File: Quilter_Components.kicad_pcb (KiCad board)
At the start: 4 copper layers, 40.4 x 100 mm, 146 parts, among them J1 Conn_01x10_Male, J2 Conn_01x10_Male, J3 Conn_01x10_Male, J4 Eurorack_10_pin_power, U1 TL072, U10 SSI2144, U2 TL074, U3 TL074, U4 TL074, U5 SSI2144, U7 SSI2144, U9 SSI2144

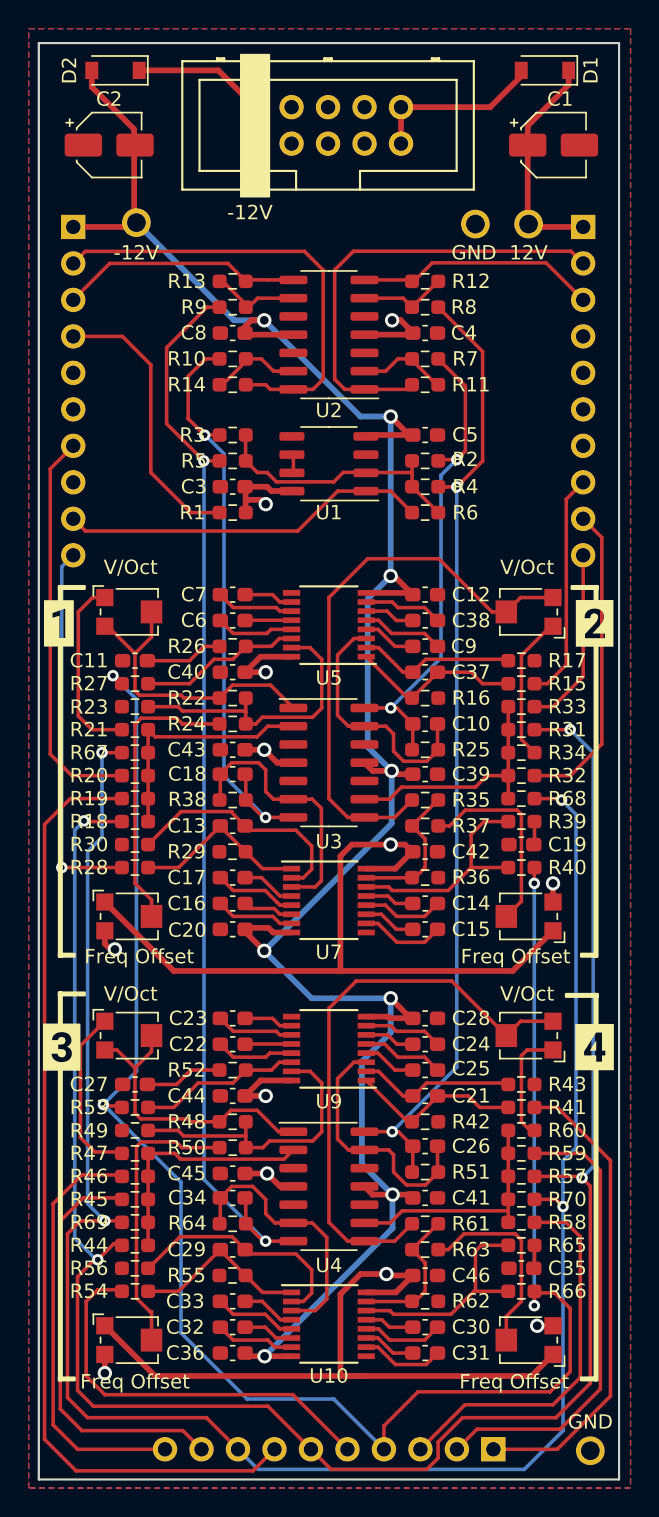
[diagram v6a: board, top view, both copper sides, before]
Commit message: Finished routing components and controls
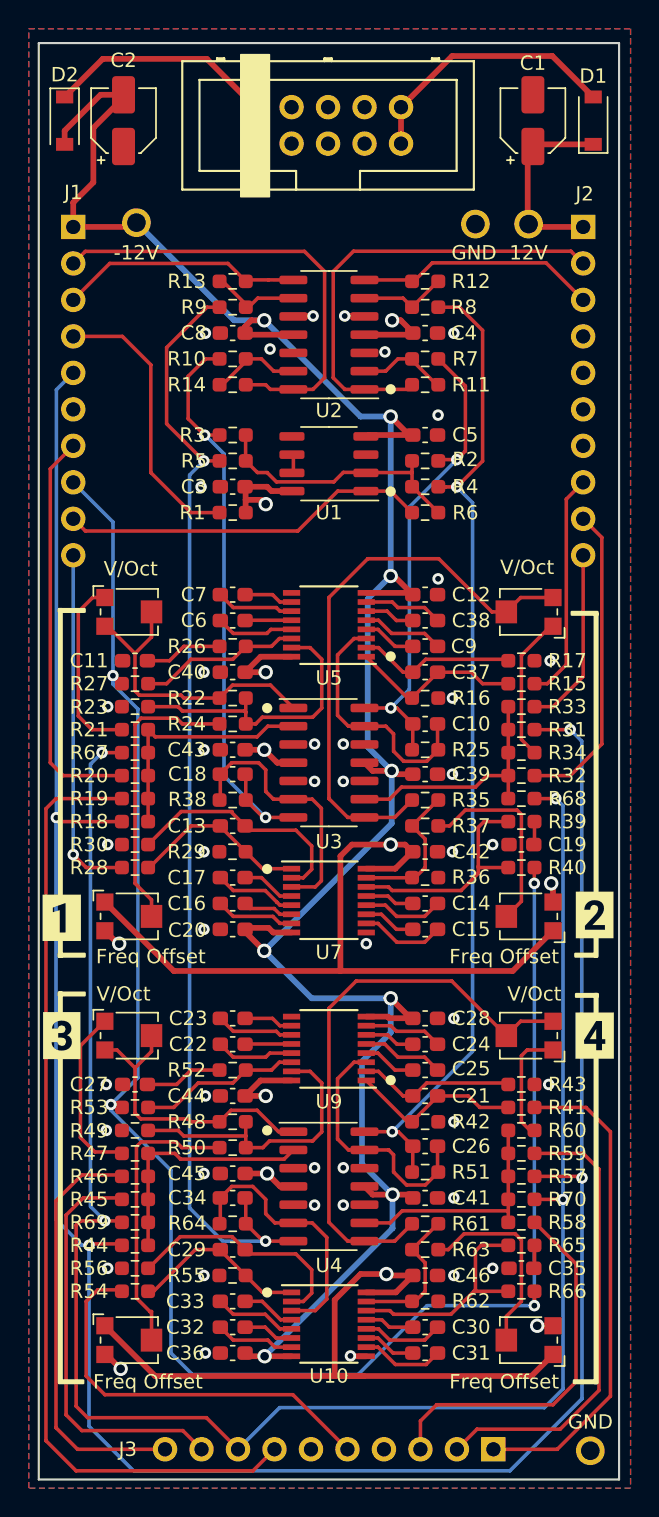
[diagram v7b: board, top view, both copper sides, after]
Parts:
- removed kibuzzard-63F9EABE: G***, kibuzzard-63F9EABE
- added kibuzzard-63FCE890: G***, kibuzzard-63FCE890, F.Cu at (51.6, 110.9)
- moved kibuzzard-63F9EC99 20.3 mm to (88.7, 110.7)
- moved D2 4.98 mm to (51.8, 55.4), turned to -90 degrees
- moved D1 4.85 mm to (88.6, 55.4), turned to 90 degrees
- moved C1 2.23 mm to (84.4, 55.4), turned to 90 degrees
- moved C2 1.97 mm to (55.9, 55.4), turned to 90 degrees
- moved kibuzzard-63F9EC4B 0.80 mm to (51.6, 119.1)
- moved kibuzzard-63F9ECEE 0.80 mm to (88.7, 119.1)
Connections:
- J1 pad 5: unconnected-(J1-Pad5) -> /FREQ_POT
- J1 pad 8: unconnected-(J1-Pad8) -> /Q_POT
- J2 pad 4: unconnected-(J2-Pad4) -> GND
- J2 pad 5: unconnected-(J2-Pad5) -> GND
- J2 pad 7: unconnected-(J2-Pad7) -> GND
- J3 pad 4: /Q_POT -> GND
- J3 pad 6: /FREQ_POT -> GND
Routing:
- net /FREQ_POT: track 139.5 -> 172.5 mm
- net /+12V_IN: track 11.7 -> 18.6 mm
- net /-12V_IN: track 11.7 -> 18.3 mm
- net -12V: track 215.8 -> 221.3 mm
- net /FREQ_JACK: track 137.0 -> 132.3 mm
- net GND: track 0.35 -> 4.23 mm, vias 0 -> 43
- net /Audio_Out4: track 77.1 -> 79.6 mm
- net /Audio_Out3: track 68.2 -> 70.0 mm
- net /AUDIO_IN2: track 26.3 -> 24.6 mm
- net /AUDIO_IN3: track 32.9 -> 34.1 mm
- net +12V: track 241.7 -> 240.5 mm
- net /Q_POT: track 124.3 -> 125.3 mm
- net /FREQ_CV1: track 66.5 -> 67.0 mm
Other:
- board text added: "J1"
- board text added: "J2"
- board text added: "J3"
- board text added: "Quilter Components v1.0 Mountjoy Modular"

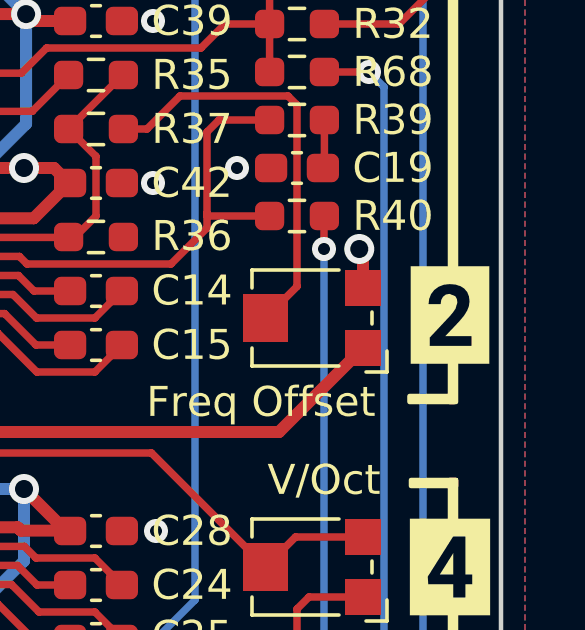
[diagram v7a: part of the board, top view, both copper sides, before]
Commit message: Schematic formatting
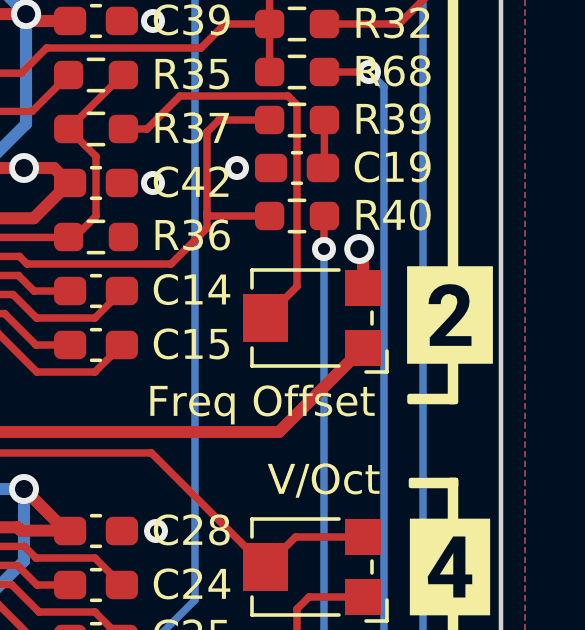
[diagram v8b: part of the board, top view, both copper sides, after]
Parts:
- removed kibuzzard-63F9EC99: G***, kibuzzard-63F9EC99
- added kibuzzard-63FCEF0D: G***, kibuzzard-63FCEF0D, F.Cu at (88.7, 110.7)
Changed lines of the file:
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@@
     )
+  )
+  (footprint "kibuzzard-63FCEF0D" (layer "F.Cu")
+    (at 88.7 110.7)
+    (descr "Generated with KiBuzzard")
+    (tags "kb_params=eyJBbGlnbm1lbnRDaG9pY2UiOiAiQ2VudGVyIiwgIkNhcExlZnRDaG9pY2UiOiAiWyIsICJDYXBSaWdodENob2ljZSI6ICJdIiwgIkZvbnRDb21ib0JveCI6ICJSb2JvdG8tQm9sZCIsICJIZWlnaHRDdHJsIjogIjEuOCIsICJMYXllckNvbWJvQm94IjogIkYuU2lsa1MiLCAiTXVsdGlMaW5lVGV4dCI6ICIyIiwgIlBhZGRpbmdCb3R0b21DdHJsIjogIjUiLCAiUGFkZGluZ0xlZnRDdHJsIjogIjYiLCAiUGFkZGluZ1JpZ2h0Q3RybCI6ICI2IiwgIlBhZGRpbmdUb3BDdHJsIjogIjUiLCAiV2lkdGhDdHJsIjogIiJ9")
+    (attr board_only exclude_from_pos_files exclude_from_bom)
+    (fp_text reference "kibuzzard-63FCEF0D" (at 0 -4.673017) (layer "F.SilkS") hide
+      (effects (font (size 0 0)))
+    )
+    (fp_text value "G***" (at 0 4.673017) (layer "F.SilkS") hide
+      (effects (font (size 0 0)))
+    )
+    (fp_poly (pts
+        (xy -0.716468 -1.625017)
+        (xy -1.430843 -1.625017)
+        (xy -1.430843 1.625017)
+        (xy -0.716468 1.625017)
+        (xy 0.716468 1.625017)
+        (xy 0.716468 1.029705)
+        (xy -0.676005 1.029705)
+        (xy -0.676005 0.753442)
+        (xy -0.018836 0.05302)
+        (xy 0.098889 -0.08546)
+        (xy 0.181384 -0.205104)
+        (xy 0.246264 -0.414393)
+        (xy 0.229172 -0.535258)
+        (xy 0.177896 -0.627171)
+        (xy -0.017441 -0.704608)
+        (xy -0.139701 -0.681063)
+        (xy -0.233009 -0.610428)
+        (xy -0.292133 -0.501423)
+        (xy -0.311841 -0.362769)
+        (xy -0.716468 -0.362769)
+        (xy -0.694318 -0.540316)
+        (xy -0.627869 -0.701818)
+        (xy -0.520957 -0.838728)
+        (xy -0.377419 -0.942501)
+        (xy -0.204755 -1.007904)
+        (xy -0.010464 -1.029705)
+        (xy 0.183245 -1.012961)
+        (xy 0.345793 -0.962732)
+        (xy 0.47718 -0.879016)
+        (xy 0.573686 -0.76476)
+        (xy 0.631589 -0.622908)
+        (xy 0.650891 -0.453461)
+        (xy 0.631357 -0.301377)
+        (xy 0.572756 -0.146503)
+        (xy 0.466716 0.022673)
+        (xy 0.304865 0.217661)
+        (xy -0.156967 0.704608)
+        (xy 0.716468 0.704608)
+        (xy 0.716468 1.029705)
+        (xy 0.716468 1.625017)
+        (xy 1.430843 1.625017)
+        (xy 1.430843 -1.625017)
+        (xy 0.716468 -1.625017)
+        (xy -0.716468 -1.625017)
+      ) (layer "F.SilkS") (width 0) (fill solid))
   )
   (footprint "Capacitor_SMD:C_0603_1608Metric_Pad1.08x0.95mm_HandSolder" (layer "F.Cu")
@@
     )
   )
-  (footprint "kibuzzard-63F9EC99" (layer "F.Cu")
-    (at 88.7 110.7)
-    (descr "Generated with KiBuzzard")
-    (tags "kb_params=eyJBbGlnbm1lbnRDaG9pY2UiOiAiQ2VudGVyIiwgIkNhcExlZnRDaG9pY2UiOiAiWyIsICJDYXBSaWdodENob2ljZSI6ICJdIiwgIkZvbnRDb21ib0JveCI6ICJSb2JvdG8tQm9sZCIsICJIZWlnaHRDdHJsIjogIjEuOCIsICJMYXllckNvbWJvQm94IjogIkYuU2lsa1MiLCAiTXVsdGlMaW5lVGV4dCI6ICIyIiwgIlBhZGRpbmdCb3R0b21DdHJsIjogIjUiLCAiUGFkZGluZ0xlZnRDdHJsIjogIjUiLCAiUGFkZGluZ1JpZ2h0Q3RybCI6ICI1IiwgIlBhZGRpbmdUb3BDdHJsIjogIjUiLCAiV2lkdGhDdHJsIjogIiJ9")
-    (attr board_only exclude_from_pos_files exclude_from_bom)
-    (fp_text reference "kibuzzard-63F9EC99" (at 0 -4.673017) (layer "F.SilkS") hide
-      (effects (font (size 0 0) (thickness 0.15)))
-    )
-    (fp_text value "G***" (at 0 4.673017) (layer "F.SilkS") hide
-      (effects (font (size 0 0) (thickness 0.15)))
-    )
-    (fp_poly (pts
-        (xy -0.716468 -1.625017)
-        (xy -1.31178 -1.625017)
-        (xy -1.31178 1.625017)
-        (xy -0.716468 1.625017)
-        (xy 0.716468 1.625017)
-        (xy 0.716468 1.029705)
-        (xy -0.676005 1.029705)
-        (xy -0.676005 0.753442)
-        (xy -0.018836 0.05302)
-        (xy 0.098889 -0.08546)
-        (xy 0.181384 -0.205104)
-        (xy 0.246264 -0.414393)
-        (xy 0.229172 -0.535258)
-        (xy 0.177896 -0.627171)
-        (xy -0.017441 -0.704608)
-        (xy -0.139701 -0.681063)
-        (xy -0.233009 -0.610428)
-        (xy -0.292133 -0.501423)
-        (xy -0.311841 -0.362769)
-        (xy -0.716468 -0.362769)
-        (xy -0.694318 -0.540316)
-        (xy -0.627869 -0.701818)
-        (xy -0.520957 -0.838728)
-        (xy -0.377419 -0.942501)
-        (xy -0.204755 -1.007904)
-        (xy -0.010464 -1.029705)
-        (xy 0.183245 -1.012961)
-        (xy 0.345793 -0.962732)
-        (xy 0.47718 -0.879016)
-        (xy 0.573686 -0.76476)
-        (xy 0.631589 -0.622908)
-        (xy 0.650891 -0.453461)
-        (xy 0.631357 -0.301377)
-        (xy 0.572756 -0.146503)
-        (xy 0.466716 0.022673)
-        (xy 0.304865 0.217661)
-        (xy -0.156967 0.704608)
-        (xy 0.716468 0.704608)
-        (xy 0.716468 1.029705)
-        (xy 0.716468 1.625017)
-        (xy 1.31178 1.625017)
-        (xy 1.31178 -1.625017)
-        (xy 0.716468 -1.625017)
-        (xy -0.716468 -1.625017)
-      ) (layer "F.SilkS") (width 0) (fill solid))
-  )
-  (footprint "Resistor_SMD:R_0603_1608Metric_Pad0.98x0.95mm_HandSolder" (layer "F.Cu")
+  (footprint "Resistor_SMD:R_0603_1608Metric_Pad0.98x0.95mm_HandSolder" (layer "F.Cu")
